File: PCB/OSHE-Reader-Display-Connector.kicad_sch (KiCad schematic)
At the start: 18 parts, among them J3 Conn_01x24_MountingPin, Q2 Si1308EDL

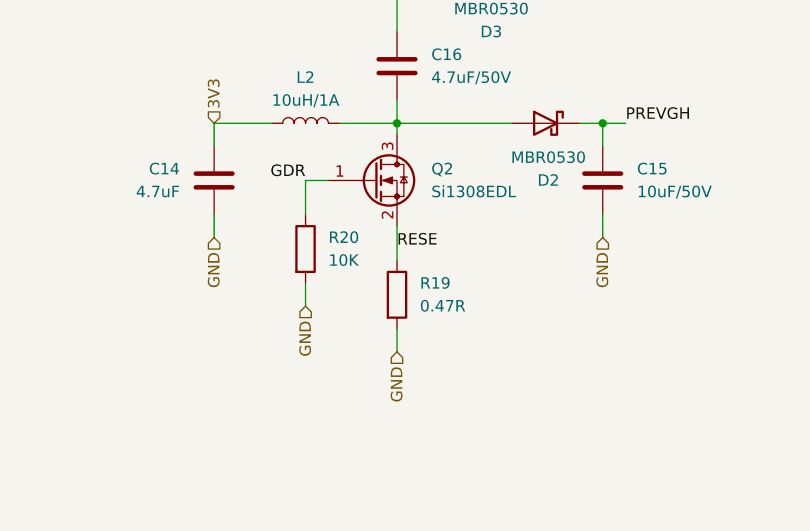
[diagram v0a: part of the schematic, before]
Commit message: Finishing touches with renaming some components and making auto BOM look cleaner
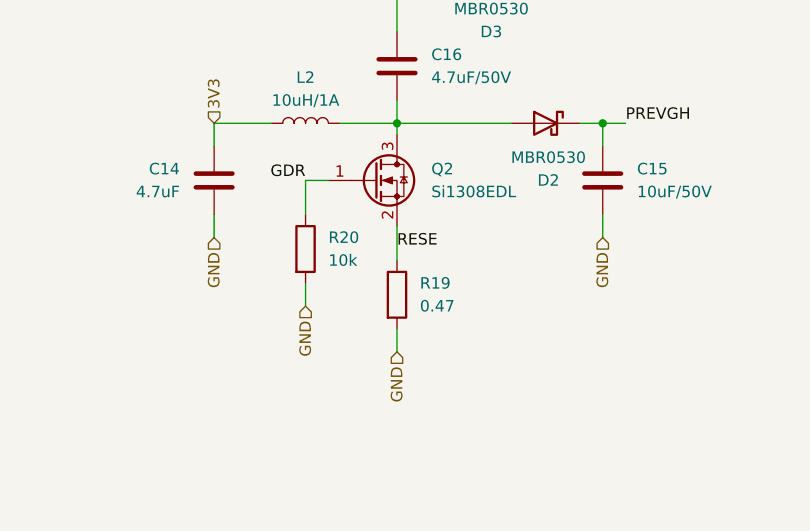
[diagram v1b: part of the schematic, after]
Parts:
- R19: value 0.47R -> 0.47
- R20: value 10K -> 10k
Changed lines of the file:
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@@
 			)
 		)
-		(property "Value" "10K"
+		(property "Value" "10k"
 			(at 40.64 74.9299 0)
 			(effects
@@
 			)
 		)
-		(property "Value" "0.47R"
+		(property "Value" "0.47"
 			(at 50.8 80.0099 0)
 			(effects
